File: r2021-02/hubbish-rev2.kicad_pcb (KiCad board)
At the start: 4 copper layers, 100 x 80 mm, 127 parts, among them J1 Conn_01x03_Male, J2 USB_A male UP, J3 USB_B_Micro (up), J4 USB_A (female down), J5 USB_A_Stacked, J6 USB_A_Stacked, J7 USB_A_Stacked, J8 Conn_01x06, Q1 Si4435, U1 2k i2c eeprom, U10 APL3511C, U11 NUP4202, U12 NUP4202, U13 NUP4202, U14 NUP4202, U15 NUP4202, U16 NUP4202, U17 NUP4202, U18 SiC437AED, U19 SE5120ST33, U2 NUP4202, U3 USB2517, U4 APL3511C, U5 APL3511C, U6 APL3511C, U7 APL3511C, U8 APL3511C, U9 APL3511C, Y1 24MHz

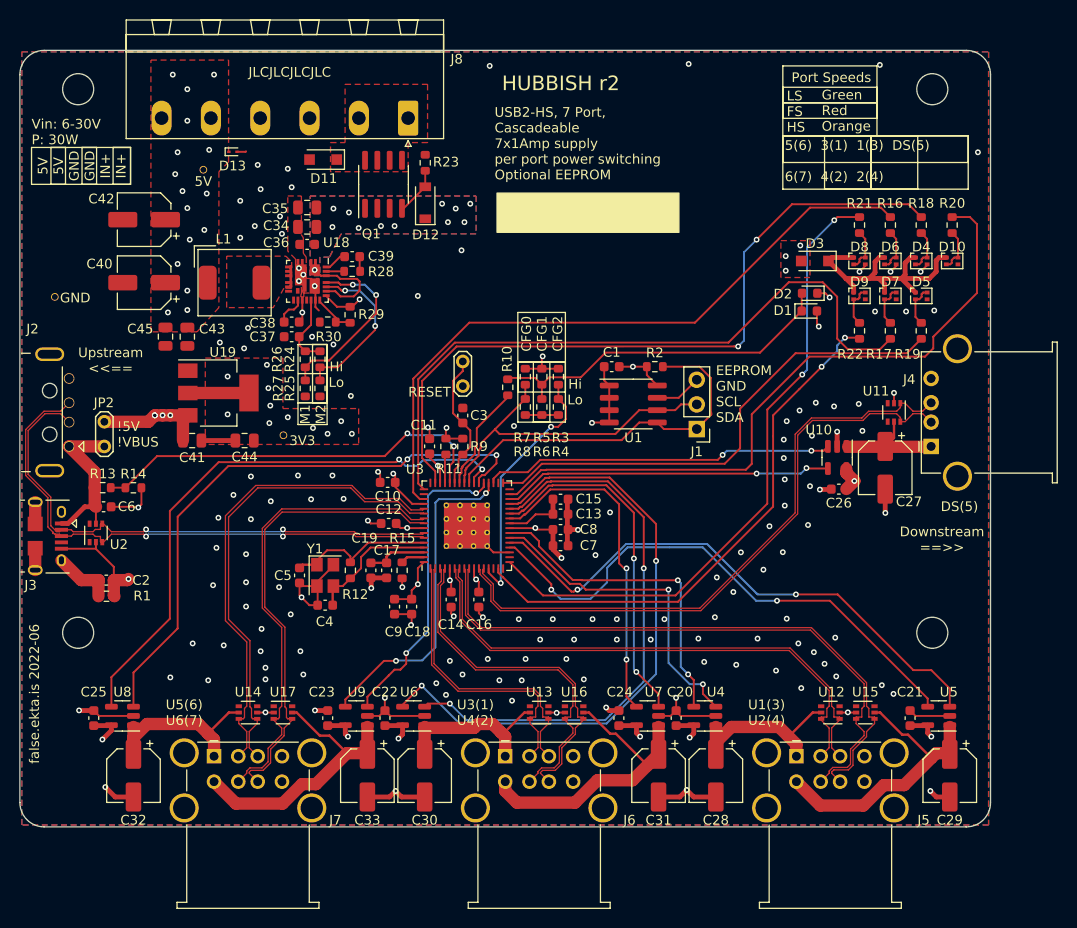
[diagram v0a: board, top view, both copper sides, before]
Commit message: BOM revisions for a rev3
Probably not going to bother even assembling rev2 pcbs.  Was missing
parts, found other things that were a little non-ideal.

Decided to start revising towards making it assembleable by JLC, so
using super cheap parts from their basic line where possible, and
minimizing bom items.
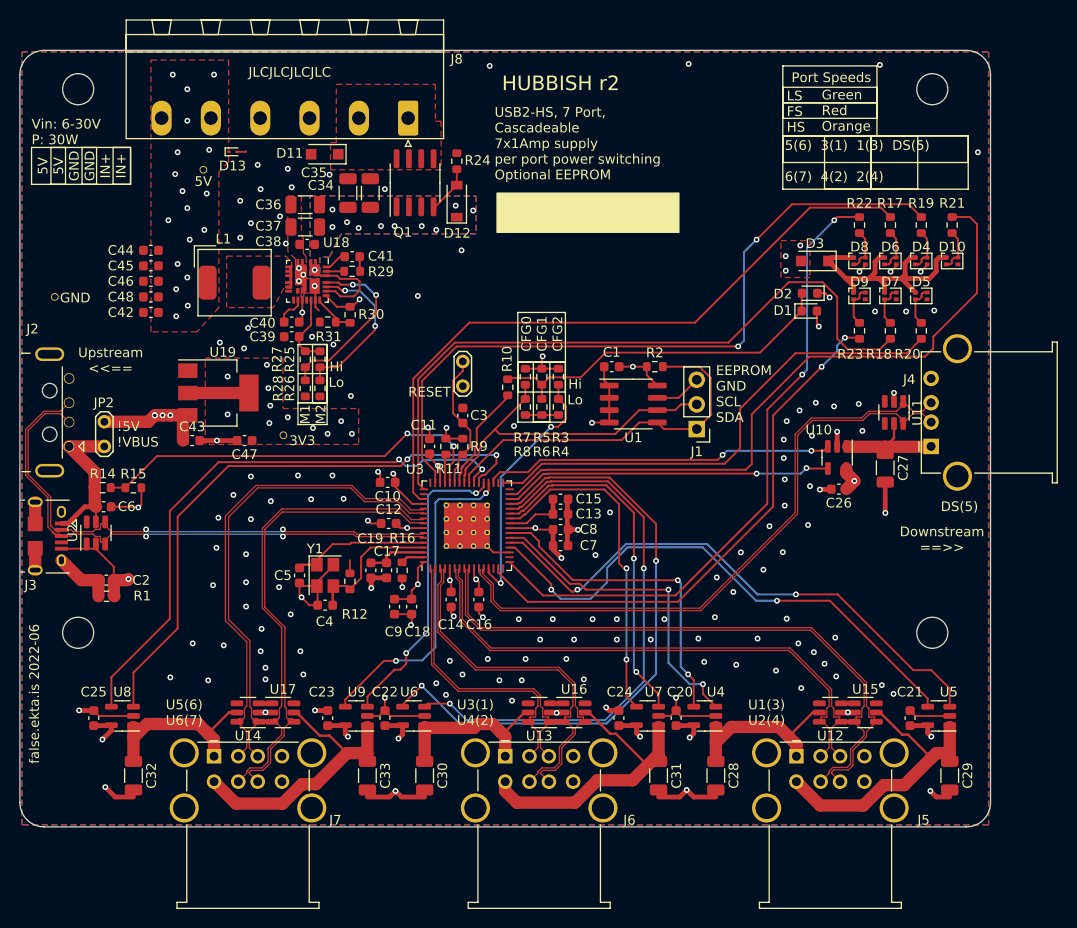
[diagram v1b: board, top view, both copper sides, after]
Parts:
- removed the C40 at (92.8, 93.9)
- removed the C43 at (97.2, 99.5)
- added C36: 10uF/30+, Capacitor_SMD:C_1206_3216Metric, F.Cu at (109.4, 85.9)
- added C37: 10uF/30+, Capacitor_SMD:C_1206_3216Metric, F.Cu at (109.4, 88.2)
- added C44: 10uF-up?, Capacitor_SMD:C_0603_1608Metric, F.Cu at (93.5, 90.6)
- added C46: 10uF-up?, Capacitor_SMD:C_0603_1608Metric, F.Cu at (93.5, 93.8)
- added C48: 10uF-up?, Capacitor_SMD:C_0603_1608Metric, F.Cu at (93.5, 95.4)
- C1, C10, C11, C12, C14, C15, C16, C18, C19, C2, C3, C8: value .1uF -> 100nF
- C27, C28, C29, C30, C31, C32, C33: footprint Capacitor_SMD:CP_Elec_5x5.4 -> Capacitor_SMD:C_1206_3216Metric
- C34, C35: value 22uF/30V+ -> 10uF/30+; footprint Capacitor_SMD:C_0805_2012Metric -> Capacitor_SMD:C_1206_3216Metric
- C38: renamed from C36; value .1uF -> 100nF/30+
- C40: renamed from C38; value 4.7uF -> 1uF
- C41: renamed from C39; value .1uF -> 100nF
- C42: value 100uF -> 100nF; footprint Capacitor_SMD:CP_Elec_5x5.4 -> Capacitor_SMD:C_0603_1608Metric
- C43: renamed from C41; footprint Capacitor_SMD:C_0805_2012Metric -> Capacitor_SMD:C_0603_1608Metric
- C45: value 22uF/6.3V -> 10uF-up?; footprint Capacitor_SMD:C_0805_2012Metric -> Capacitor_SMD:C_0603_1608Metric
- C47: renamed from C44; footprint Capacitor_SMD:C_0805_2012Metric -> Capacitor_SMD:C_0603_1608Metric
- C6: value 2.2uF -> 1uF
- R28: renamed from R27; value 499k -> 510k
- R29: renamed from R28; value 2.2 -> 0
- R30: renamed from R29; value 22k -> 75k
- R31: renamed from R30; value 3k -> 10k
- U11, U12, U13, U14, U15, U16, U17, U2: footprint Package_TO_SOT_SMD:SOT-363_SC-70-6 -> Package_TO_SOT_SMD:SOT-23-6
- moved C42 9.59 mm to (93.5, 97.0)
- moved C45 7.45 mm to (93.5, 92.2), turned to 180 degrees
- moved C34 7.38 mm to (116.1, 84.7), turned to 90 degrees
- moved C35 4.46 mm to (113.8, 84.7), turned to 90 degrees
- moved Q1 3.26 mm to (120.7, 83.6)
- moved D12 3.26 mm to (125.0, 85.5)
- moved R24 3.26 mm to (125.0, 81.4)
- moved R12 1.13 mm to (114.0, 124.7)
- moved D11 0.57 mm to (111.4, 80.7)
- renumbered C37 to C39, R13 to R14, R14 to R15, R15 to R16, R16 to R17, R17 to R18, R18 to R19, R19 to R20, R20 to R21, R21 to R22, R22 to R23, R23 to R24, R24 to R25, R25 to R26, R26 to R27
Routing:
- net /upstream-config-leds/xtal1: track 13.6 -> 14.5 mm
- net GND: track 136.1 -> 136.4 mm, vias 145 -> 148
- net +VDC: vias 12 -> 11
- net +5V: vias 28 -> 30
